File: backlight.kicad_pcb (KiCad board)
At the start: 2 copper layers, 150 x 90 mm, 52 parts, among them J1 Screw_Terminal_01x03, U1 SY7203

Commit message: Reroute board
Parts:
- added R7: 10k, Resistor_SMD:R_0805_2012Metric, F.Cu at (68.6, 61.9)
- C1: value C -> 4.7uF 35V
- C2: value C -> 2.2uF 35V
- D41: value D_Schottky -> SS24
- J1: value Screw_Terminal_01x03 -> Conn_01x03_MountingPin; footprint Connector_PinHeader_2.54mm:PinHeader_1x03_P2.54mm_Vertical_SMD_Pin1Left -> rainwalker:XH254-0,5-3-2,5-V-SMD_1x03-1MP_P2.50mm_Vertical
- R6: value R -> 2R
- U1: footprint Package_DFN_QFN:DFN-10-1EP_3x3mm_P0.5mm_EP1.75x2.7mm -> rainwalker:SY7203DBC-DFN-10-1EP_3x3mm_P0.5mm_EP1.75x2.7mm
- moved C2 26.6 mm to (82.1, 62.8), turned to 180 degrees
- moved D41 26.5 mm to (84.7, 58.2)
- moved R6 14.3 mm to (81.6, 65.5)
- moved C1 14.0 mm to (75.0, 63.8)
- moved L1 14.0 mm to (78.5, 58.1)
- moved U1 14.0 mm to (78.3, 63.5)
- moved J1 12.0 mm to (61.8, 61.0), turned to 90 degrees
- moved R5 4.10 mm to (191.9, 127.1), turned to 0 degrees
- moved R4 2.49 mm to (191.9, 114.0), turned to 0 degrees
- moved R3 2.39 mm to (191.9, 94.0), turned to 0 degrees
- moved R1 1.91 mm to (191.9, 54.1), turned to 0 degrees
- moved R2 1.48 mm to (191.9, 74.0), turned to 0 degrees
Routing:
- net /LED-: track 200.6 -> 0.00 mm
- net /LED+: track 97.4 -> 21.1 mm
- net GND: track 19.9 -> 0.00 mm
- net Net-(D41-A): track 18.4 -> 0.00 mm
- net VPP: track 16.7 -> 0.00 mm
- net /EN_PWM: track 15.9 -> 12.6 mm
- net Net-(D40-K): track 6.60 -> 4.42 mm
- net Net-(D32-K): track 5.89 -> 4.04 mm
- net Net-(D16-K): track 3.43 -> 4.04 mm
- added copper zone on F.Cu, net /LED-
- added copper zone on F.Cu, net Net-(D41-A)

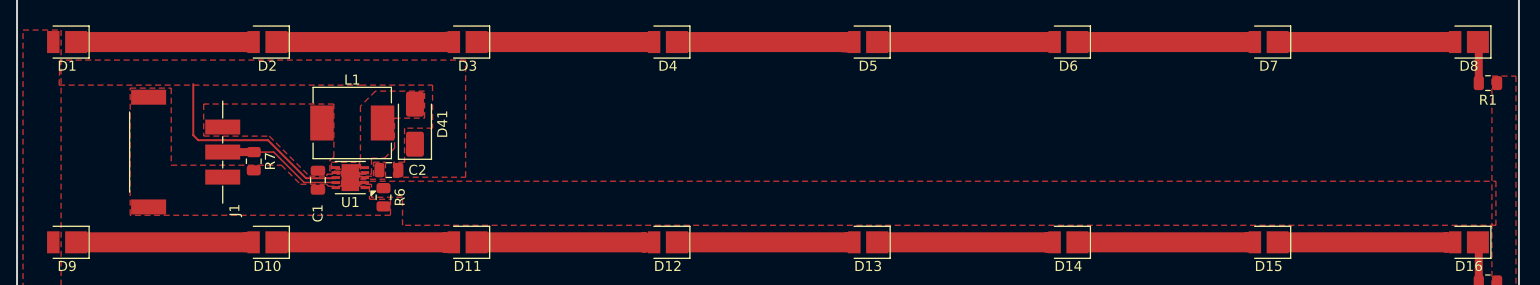
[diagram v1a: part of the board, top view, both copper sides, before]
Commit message: Update backlight.kicad_pcb
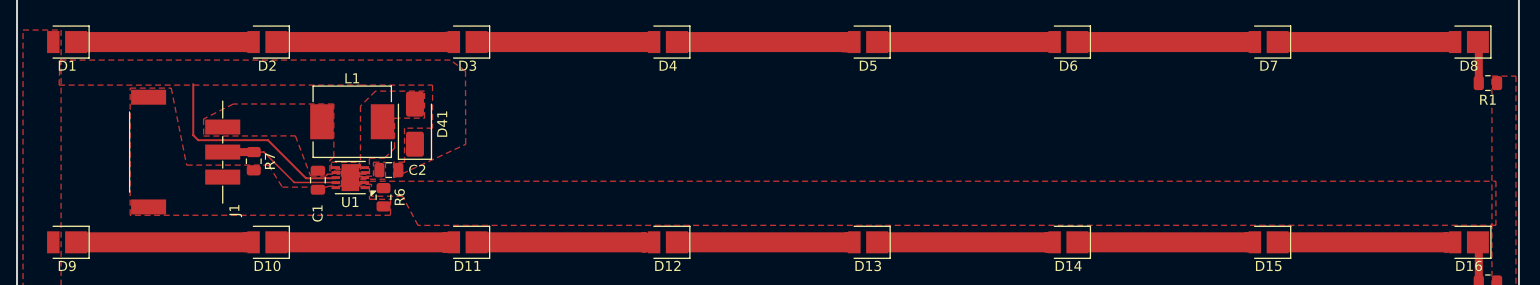
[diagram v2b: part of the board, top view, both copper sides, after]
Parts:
- moved L1 0.12 mm to (78.5, 58.0)
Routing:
- net /EN_PWM: track 12.6 -> 13.4 mm
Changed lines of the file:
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@@
 	(footprint "Inductor_SMD:L_Chilisin_BMRx00060630"
 		(layer "F.Cu")
-		(at 78.479 58.0835)
+		(at 78.479 57.96)
 		(descr "Inductor, Chilisin, BMRx00060630, 7.3x6.6x3.0mm, https://www.chilisin.com/upload/media/product/power/file/BMRx_Series.pdf")
 		(tags "Inductor bmrx mchi")
@@
 	)
 	(segment
-		(start 76.8215 64.0235)
-		(end 73.6735 64.0235)
+		(start 65.543 60.9875)
+		(end 68.643 60.9875)
+		(width 0.8)
+		(layer "F.Cu")
+		(net 43)
+	)
+	(segment
+		(start 68.6105 61.02)
+		(end 67.7855 61.02)
 		(width 0.15)
 		(layer "F.Cu")
@@
 	)
 	(segment
-		(start 73.6735 64.0235)
-		(end 70.6375 60.9875)
+		(start 76.8355 64.0375)
+		(end 76.8215 64.0235)
 		(width 0.15)
 		(layer "F.Cu")
@@
 	)
 	(segment
-		(start 65.543 60.9875)
+		(start 69.6575 60.9875)
 		(end 68.643 60.9875)
-		(width 0.8)
+		(width 0.15)
 		(layer "F.Cu")
 		(net 43)
 	)
 	(segment
-		(start 70.6375 60.9875)
+		(start 68.6455 60.99)
 		(end 68.643 60.9875)
 		(width 0.15)
@@
 	)
 	(segment
-		(start 76.8355 64.0375)
-		(end 76.8215 64.0235)
+		(start 72.6935 64.0235)
+		(end 69.6575 60.9875)
+		(width 0.15)
+		(layer "F.Cu")
+		(net 43)
+	)
+	(segment
+		(start 76.8215 64.0235)
+		(end 72.6935 64.0235)
+		(width 0.15)
+		(layer "F.Cu")
+		(net 43)
+	)
+	(segment
+		(start 68.643 60.9875)
+		(end 68.6105 61.02)
 		(width 0.15)
 		(layer "F.Cu")
@@
 			(pts
 				(xy 49.2 54.3) (xy 79.3 54.3) (xy 86.5 54.3) (xy 86.5 58.6) (xy 83.7 58.6) (xy 83.7 62) (xy 82.6 62)
-				(xy 82.6 63.5) (xy 89.8 63.5) (xy 89.8 51.8) (xy 49.3 51.8)
+				(xy 82.61 63.55) (xy 89.79 60.23) (xy 89.81 60.19) (xy 89.79 52.9) (xy 88.28 51.8) (xy 49.3 51.8)
 			)
 		)
@@
 		(polygon
 			(pts
-				(xy 79.3 56.4) (xy 79.3 63.2) (xy 80.4 63.2) (xy 80.4 61.6) (xy 81.7 61.6) (xy 82.7 60.6) (xy 82.7 57.6)
+				(xy 79.3 56.4) (xy 79.3 63.2) (xy 80.2 63.2) (xy 80.19 61.6) (xy 81.7 61.6) (xy 82.7 60.6) (xy 82.7 57.6)
 				(xy 85.7 57.6) (xy 85.7 54.9) (xy 80.8 54.9)
 			)
@@
 		(min_thickness 0.2)
 		(filled_areas_thickness no)
-		(fill yes
+		(fill
 			(thermal_gap 0.5)
 			(thermal_bridge_width 0.5)
@@
 		(polygon
 			(pts
-				(xy 63.643 59.3875) (xy 70.2 59.4) (xy 74.2 63.4) (xy 75.943 63.3875) (xy 75.943 63.1875) (xy 77.243 63.1875)
+				(xy 63.643 59.3875) (xy 72.8 59.37) (xy 74.32 63.38) (xy 75.943 63.3875) (xy 75.943 63.1875) (xy 77.243 63.1875)
 				(xy 77.243 62.8875) (xy 76.243 62.8875) (xy 76.243 61.7875) (xy 76.643 61.5) (xy 76.643 56.1875)
-				(xy 63.643 56.1875)
+				(xy 66.6 56.1875) (xy 63.63 57.68)
 			)
 		)
@@
 		(polygon
 			(pts
-				(xy 82.3 65.7) (xy 82.3 67.3) (xy 56.3 67.3) (xy 56.3 54.6) (xy 60.4 54.6) (xy 60.4 62.3) (xy 71.4 62.3)
-				(xy 73.3 64.2) (xy 75.9 64.2) (xy 76.1 64.4) (xy 77.4 64.4) (xy 77.4 62.7) (xy 76.4 62.7) (xy 76.4 62)
+				(xy 82.3 65.7) (xy 82.3 67.3) (xy 56.3 67.3) (xy 56.3 54.6) (xy 60.4 54.6) (xy 61.94 62.29) (xy 70.12 62.29)
+				(xy 71.5 64.49) (xy 75.91 64.49) (xy 76.1 64.4) (xy 77.4 64.4) (xy 77.4 62.7) (xy 76.4 62.7) (xy 76.4 62)
 				(xy 79.2 62) (xy 79.2 64.4) (xy 80.2 64.4) (xy 80.2 65.7)
 			)
@@
 		(polygon
 			(pts
-				(xy 80.4 64.2) (xy 79.3 64.2) (xy 79.3 63.9) (xy 192.7 63.9) (xy 192.7 68.3) (xy 83.5 68.3) (xy 83.5 65.5)
-				(xy 80.4 65.5)
+				(xy 80.4 64.2) (xy 79.3 64.2) (xy 79.3 63.9) (xy 192.7 63.9) (xy 192.7 68.3) (xy 85.05 68.31) (xy 83.5 65.4)
+				(xy 80.4 65.4)
 			)
 		)
